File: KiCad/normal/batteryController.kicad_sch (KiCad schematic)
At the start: 20 parts, among them J1 Screw_Terminal_01x02, J2 Conn_01x04_Male, J3 Conn_01x04_Male, J4 Conn_01x04_Male, J5 Conn_02x04_Odd_Even, J6 Conn_01x01_Male, J7 USB_A, U1 ATtiny45V-10P, U2 LM2596S-ADJ, U3 LP2950-3.3_TO92

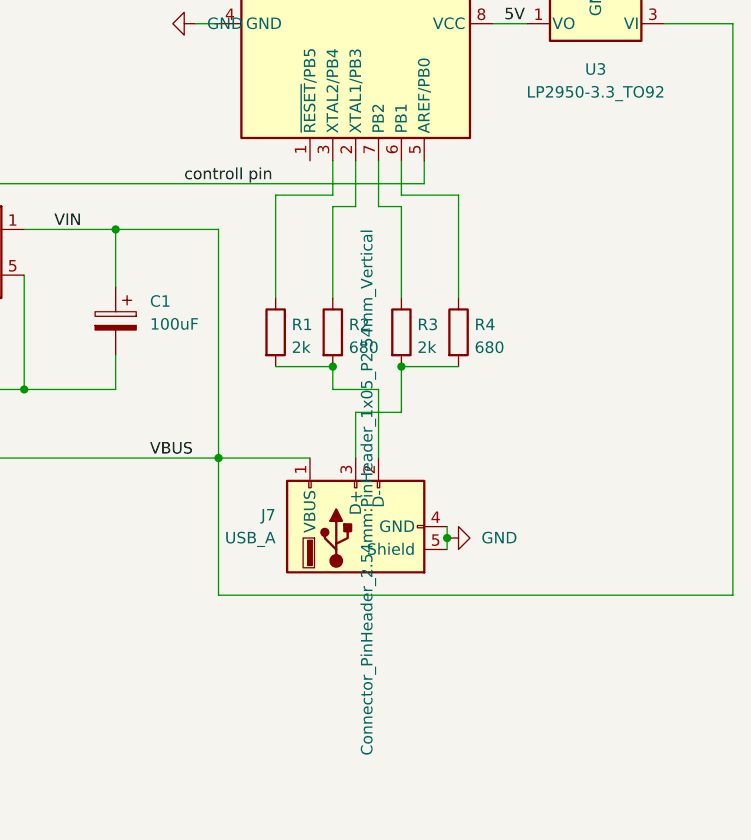
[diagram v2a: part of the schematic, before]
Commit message: spaced out more for pcb milling
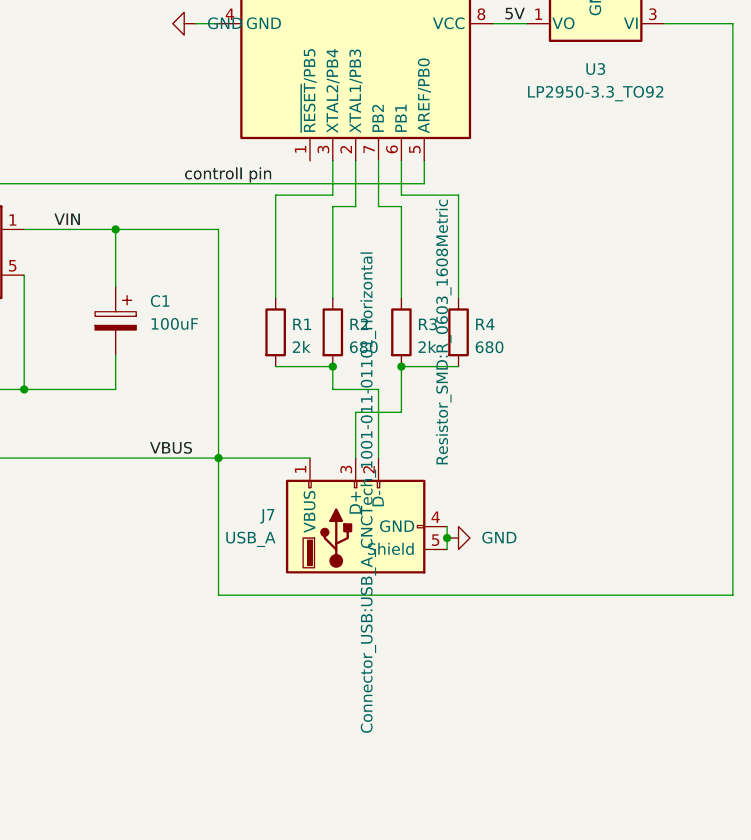
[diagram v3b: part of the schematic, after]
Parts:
- D1: footprint Diode_THT:D_DO-41_SOD81_P7.62mm_Horizontal -> Diode_SMD:D_1206_3216Metric
- J7: footprint Connector_PinHeader_2.54mm:PinHeader_1x05_P2.54mm_Vertical -> Connector_USB:USB_A_CNCTech_1001-011-01101_Horizontal
- R1, R2, R3, R4: footprint Resistor_THT:R_Axial_DIN0207_L6.3mm_D2.5mm_P7.62mm_Horizontal -> Resistor_SMD:R_0603_1608Metric
- U3: footprint Package_TO_SOT_THT:TO-92_Inline -> Package_TO_SOT_SMD:SOT-89-3
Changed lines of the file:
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@@
     (property "Reference" "U3" (id 0) (at 215.9 71.12 0))
     (property "Value" "LP2950-3.3_TO92" (id 1) (at 215.9 73.66 0))
-    (property "Footprint" "Package_TO_SOT_THT:TO-92_Inline" (id 2) (at 215.9 71.755 0)
+    (property "Footprint" "Package_TO_SOT_SMD:SOT-89-3" (id 2) (at 215.9 71.755 0)
       (effects (font (size 1.27 1.27) italic) hide)
     )
@@
       (effects (font (size 1.27 1.27)) (justify left))
     )
-    (property "Footprint" "Resistor_THT:R_Axial_DIN0207_L6.3mm_D2.5mm_P7.62mm_Horizontal" (id 2) (at 198.882 100.33 90)
-      (effects (font (size 1.27 1.27)) hide)
-    )
+    (property "Footprint" "Resistor_SMD:R_0603_1608Metric" (id 2) (at 198.882 100.33 90))
     (property "Datasheet" "~" (id 3) (at 200.66 100.33 0)
       (effects (font (size 1.27 1.27)) hide)
@@
       (effects (font (size 1.27 1.27)) (justify left))
     )
-    (property "Footprint" "Diode_THT:D_DO-41_SOD81_P7.62mm_Horizontal" (id 2) (at 123.19 101.6 0)
+    (property "Footprint" "Diode_SMD:D_1206_3216Metric" (id 2) (at 123.19 101.6 0)
       (effects (font (size 1.27 1.27)) hide)
     )
@@
       (effects (font (size 1.27 1.27)) (justify left))
     )
-    (property "Footprint" "Connector_PinHeader_2.54mm:PinHeader_1x05_P2.54mm_Vertical" (id 2) (at 190.5 118.11 0))
+    (property "Footprint" "Connector_USB:USB_A_CNCTech_1001-011-01101_Horizontal" (id 2) (at 190.5 118.11 0))
     (property "Datasheet" " ~" (id 3) (at 190.5 118.11 0)
       (effects (font (size 1.27 1.27)) hide)
@@
       (effects (font (size 1.27 1.27)) (justify left))
     )
-    (property "Footprint" "Resistor_THT:R_Axial_DIN0207_L6.3mm_D2.5mm_P7.62mm_Horizontal" (id 2) (at 184.912 100.33 90)
+    (property "Footprint" "Resistor_SMD:R_0603_1608Metric" (id 2) (at 184.912 100.33 90)
       (effects (font (size 1.27 1.27)) hide)
     )
@@
       (effects (font (size 1.27 1.27)) (justify left))
     )
-    (property "Footprint" "Resistor_THT:R_Axial_DIN0207_L6.3mm_D2.5mm_P7.62mm_Horizontal" (id 2) (at 178.562 100.33 90)
+    (property "Footprint" "Resistor_SMD:R_0603_1608Metric" (id 2) (at 178.562 100.33 90)
       (effects (font (size 1.27 1.27)) hide)
     )
@@
       (effects (font (size 1.27 1.27)) (justify left))
     )
-    (property "Footprint" "Resistor_THT:R_Axial_DIN0207_L6.3mm_D2.5mm_P7.62mm_Horizontal" (id 2) (at 192.532 100.33 90)
+    (property "Footprint" "Resistor_SMD:R_0603_1608Metric" (id 2) (at 192.532 100.33 90)
       (effects (font (size 1.27 1.27)) hide)
     )
@@
     )
     (path "/1d13f9ff-2d62-4408-a35a-4129e8a46621"
-      (reference "D1") (unit 1) (value "D_Schottky") (footprint "Diode_THT:D_DO-41_SOD81_P7.62mm_Horizontal")
+      (reference "D1") (unit 1) (value "D_Schottky") (footprint "Diode_SMD:D_1206_3216Metric")
     )
     (path "/c9ab3aec-242e-41c2-b166-94dff047d4f7"
@@
     )
     (path "/25de26c2-41dc-4960-a69d-42850e5c883f"
-      (reference "J7") (unit 1) (value "USB_A") (footprint "Connector_PinHeader_2.54mm:PinHeader_1x05_P2.54mm_Vertical")
+      (reference "J7") (unit 1) (value "USB_A") (footprint "Connector_USB:USB_A_CNCTech_1001-011-01101_Horizontal")
     )
     (path "/1abafb25-b28e-4be5-8607-42abf1f09db7"
@@
     )
     (path "/efbd3197-cbc9-408a-a2b5-e8292a952aae"
-      (reference "R1") (unit 1) (value "2k") (footprint "Resistor_THT:R_Axial_DIN0207_L6.3mm_D2.5mm_P7.62mm_Horizontal")
+      (reference "R1") (unit 1) (value "2k") (footprint "Resistor_SMD:R_0603_1608Metric")
     )
     (path "/4fd71c9f-fda7-44dc-a730-71f9a293687a"
-      (reference "R2") (unit 1) (value "680") (footprint "Resistor_THT:R_Axial_DIN0207_L6.3mm_D2.5mm_P7.62mm_Horizontal")
+      (reference "R2") (unit 1) (value "680") (footprint "Resistor_SMD:R_0603_1608Metric")
     )
     (path "/f6c853d4-bbcd-4b7b-9a09-2cb0aa558725"
-      (reference "R3") (unit 1) (value "2k") (footprint "Resistor_THT:R_Axial_DIN0207_L6.3mm_D2.5mm_P7.62mm_Horizontal")
+      (reference "R3") (unit 1) (value "2k") (footprint "Resistor_SMD:R_0603_1608Metric")
     )
     (path "/136ccffd-861c-43d7-9c0d-f960a50fef7f"
-      (reference "R4") (unit 1) (value "680") (footprint "Resistor_THT:R_Axial_DIN0207_L6.3mm_D2.5mm_P7.62mm_Horizontal")
+      (reference "R4") (unit 1) (value "680") (footprint "Resistor_SMD:R_0603_1608Metric")
     )
     (path "/03e9cf85-6335-4a1e-94d1-32f0508de303"
@@
     )
     (path "/0630a5b9-6e05-4f50-8a4d-d803ec7f325f"
-      (reference "U3") (unit 1) (value "LP2950-3.3_TO92") (footprint "Package_TO_SOT_THT:TO-92_Inline")
-    )
-  )
+      (reference "U3") (unit 1) (value "LP2950-3.3_TO92") (footprint "Package_TO_SOT_SMD:SOT-89-3")
+    )
+  )
